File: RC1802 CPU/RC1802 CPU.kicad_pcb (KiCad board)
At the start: 2 copper layers, 99.1 x 99.1 mm, 50 parts, among them J1 Mount, J2 Mount, J3 Mount, J4 Mount, J5 CONN_01X39, J6 CONN_02X20, J7 BARREL_JACK, J8 Conn_CLK, J9 Conn_Q, U1 74LS04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

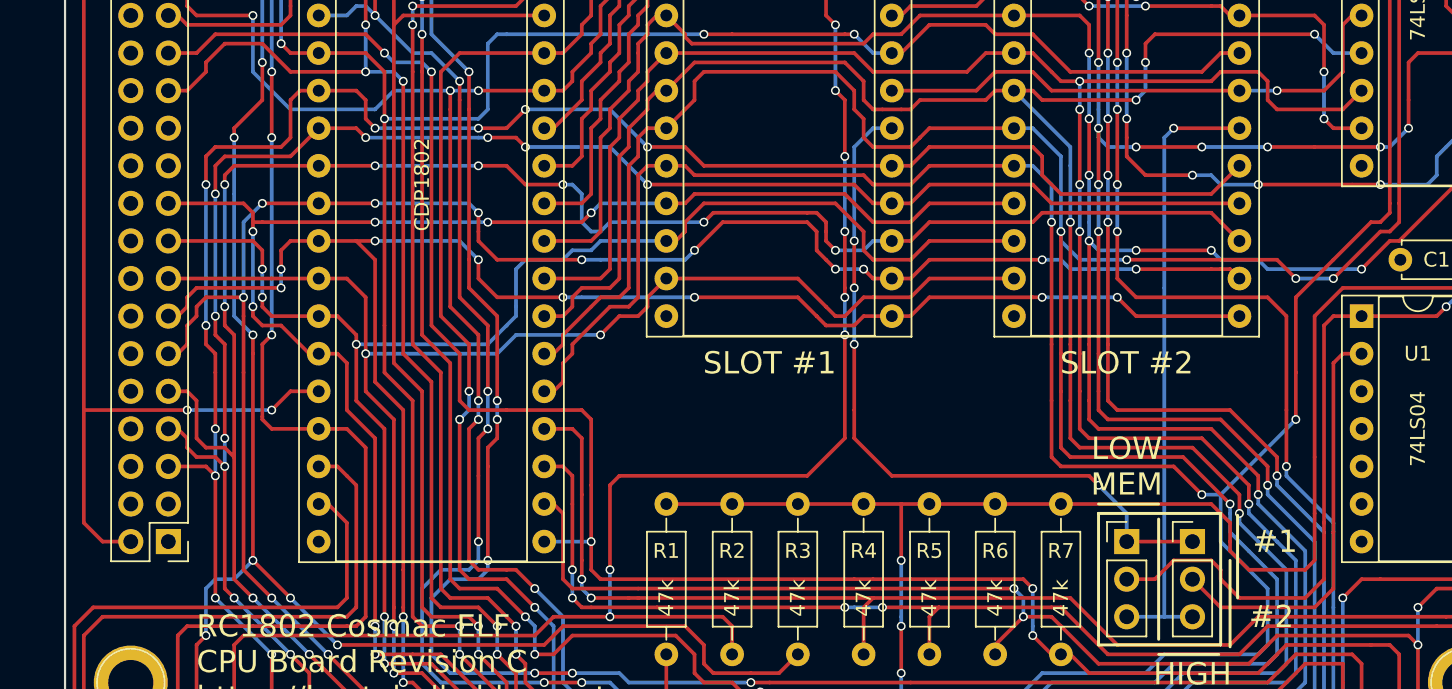
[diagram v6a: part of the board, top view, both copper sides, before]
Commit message: Added ~Q to UI connector
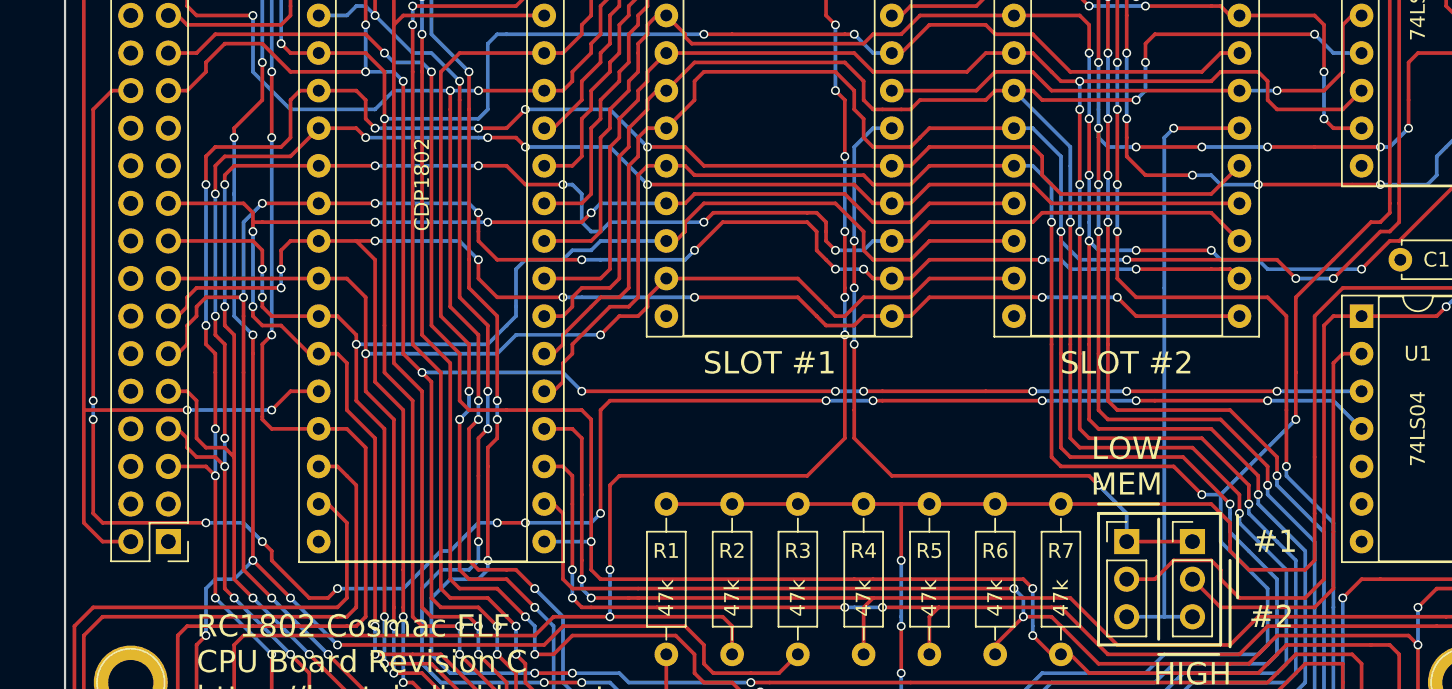
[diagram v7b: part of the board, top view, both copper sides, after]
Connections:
- J6 pad 26: GND -> /~Q
- U1 pad 3: GND -> Q
- U1 pad 4: (no net) -> /~Q
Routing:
- net /~Q: track 0.00 -> 129.2 mm, vias 0 -> 13
- net Q: track 241.1 -> 305.1 mm, vias 9 -> 16
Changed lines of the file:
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@@
     (links 232)
     (no_connects 0)
-    (area 94.275 39.757856 201.735 156.825001)
+    (area 100.209871 48.184999 199.465001 147.395001)
     (thickness 1.6)
     (drawings 150)
-    (tracks 2172)
+    (tracks 2238)
     (zones 0)
     (modules 50)
-    (nets 70)
+    (nets 71)
   )
   (page A4)
@@
   (net 68 "Net-(J8-Pad2)")
   (net 69 "Net-(J8-Pad4)")
+  (net 70 /~Q)
   (net_class Default "This is the default net class."
     (clearance 0.2)
@@
     (add_net /MA8)
     (add_net /MA9)
+    (add_net /~Q)
     (add_net CLOCK)
     (add_net DMA_IN)
@@
       (net 1 GND))
     (pad 3 thru_hole oval (at 0 5.08) (size 1.6 1.6) (drill 0.8) (layers *.Cu *.Mask)
-      (net 1 GND))
+      (net 23 Q))
     (pad 10 thru_hole oval (at 7.62 10.16) (size 1.6 1.6) (drill 0.8) (layers *.Cu *.Mask))
-    (pad 4 thru_hole oval (at 0 7.62) (size 1.6 1.6) (drill 0.8) (layers *.Cu *.Mask))
+    (pad 4 thru_hole oval (at 0 7.62) (size 1.6 1.6) (drill 0.8) (layers *.Cu *.Mask)
+      (net 70 /~Q))
     (pad 11 thru_hole oval (at 7.62 7.62) (size 1.6 1.6) (drill 0.8) (layers *.Cu *.Mask)
       (net 1 GND))
@@
       (net 23 Q))
     (pad 26 thru_hole oval (at 2.54 30.48 180) (size 1.7 1.7) (drill 1) (layers *.Cu *.Mask)
-      (net 1 GND))
+      (net 70 /~Q))
     (pad 27 thru_hole oval (at 0 33.02 180) (size 1.7 1.7) (drill 1) (layers *.Cu *.Mask)
       (net 3 EF4))
@@
   (segment (start 144.145 142.24) (end 140.97 142.24) (width 0.25) (layer F.Cu) (net 22))
   (segment (start 144.78 142.875) (end 144.78 146.05) (width 0.25) (layer F.Cu) (net 22))
+  (segment (start 155.575 121.92) (end 154.305 121.92) (width 0.25) (layer F.Cu) (net 23))
+  (segment (start 187.96 121.92) (end 184.785 121.92) (width 0.25) (layer B.Cu) (net 23))
+  (segment (start 165.735 121.92) (end 162.56 121.92) (width 0.25) (layer F.Cu) (net 23))
+  (via (at 165.735 121.92) (size 0.6) (drill 0.4) (layers F.Cu B.Cu) (net 23))
+  (segment (start 172.085 121.92) (end 165.735 121.92) (width 0.25) (layer B.Cu) (net 23))
+  (via (at 172.085 121.92) (size 0.6) (drill 0.4) (layers F.Cu B.Cu) (net 23))
+  (segment (start 182.245 121.92) (end 172.085 121.92) (width 0.25) (layer F.Cu) (net 23))
+  (via (at 182.245 121.92) (size 0.6) (drill 0.4) (layers F.Cu B.Cu) (net 23))
+  (segment (start 184.785 121.92) (end 182.245 121.92) (width 0.25) (layer B.Cu) (net 23))
+  (segment (start 155.575 121.92) (end 162.56 121.92) (width 0.25) (layer F.Cu) (net 23))
+  (via (at 124.46 120.65) (size 0.6) (drill 0.4) (layers F.Cu B.Cu) (net 23))
+  (segment (start 133.985 120.65) (end 124.46 120.65) (width 0.25) (layer B.Cu) (net 23))
+  (segment (start 135.255 121.92) (end 133.985 120.65) (width 0.25) (layer B.Cu) (net 23))
+  (via (at 135.255 121.92) (size 0.6) (drill 0.4) (layers F.Cu B.Cu) (net 23))
+  (segment (start 152.4 121.92) (end 135.255 121.92) (width 0.25) (layer F.Cu) (net 23))
+  (via (at 152.4 121.92) (size 0.6) (drill 0.4) (layers F.Cu B.Cu) (net 23))
+  (segment (start 154.305 121.92) (end 152.4 121.92) (width 0.25) (layer B.Cu) (net 23))
+  (via (at 154.305 121.92) (size 0.6) (drill 0.4) (layers F.Cu B.Cu) (net 23))
   (segment (start 184.15 48.895) (end 186.055 48.895) (width 0.25) (layer F.Cu) (net 23))
   (via (at 100.965 80.01) (size 0.6) (drill 0.4) (layers F.Cu B.Cu) (net 23))
@@
   (via (at 123.19 100.965) (size 0.6) (drill 0.4) (layers F.Cu B.Cu) (net 23))
   (segment (start 123.19 119.38) (end 123.19 100.965) (width 0.25) (layer F.Cu) (net 23))
-  (segment (start 125.095 121.285) (end 123.19 119.38) (width 0.25) (layer F.Cu) (net 23))
+  (segment (start 125.095 121.285) (end 124.46 120.65) (width 0.25) (layer F.Cu) (net 23))
+  (segment (start 124.46 120.65) (end 123.19 119.38) (width 0.25) (layer F.Cu) (net 23))
   (segment (start 125.095 135.89) (end 125.095 121.285) (width 0.25) (layer F.Cu) (net 23))
   (segment (start 125.73 136.525) (end 125.095 135.89) (width 0.25) (layer F.Cu) (net 23))
@@
   (via (at 128.27 68.58) (size 0.6) (drill 0.4) (layers F.Cu B.Cu) (net 69))
   (segment (start 129.54 67.31) (end 128.27 68.58) (width 0.25) (layer B.Cu) (net 69))
+  (segment (start 118.745 135.255) (end 123.19 135.255) (width 0.25) (layer B.Cu) (net 70))
+  (segment (start 112.395 130.81) (end 113.665 132.08) (width 0.25) (layer B.Cu) (net 70))
+  (via (at 113.665 132.08) (size 0.6) (drill 0.4) (layers F.Cu B.Cu) (net 70))
+  (segment (start 113.665 132.08) (end 114.3 132.715) (width 0.25) (layer F.Cu) (net 70))
+  (segment (start 114.3 132.715) (end 114.3 133.35) (width 0.25) (layer F.Cu) (net 70))
+  (segment (start 114.3 133.35) (end 116.84 135.89) (width 0.25) (layer F.Cu) (net 70))
+  (segment (start 116.84 135.89) (end 118.11 135.89) (width 0.25) (layer F.Cu) (net 70))
+  (segment (start 118.11 135.89) (end 118.745 135.255) (width 0.25) (layer F.Cu) (net 70))
+  (via (at 118.745 135.255) (size 0.6) (drill 0.4) (layers F.Cu B.Cu) (net 70))
+  (segment (start 124.46 133.985) (end 125.73 132.715) (width 0.25) (layer B.Cu) (net 70))
+  (segment (start 125.73 132.715) (end 126.365 132.715) (width 0.25) (layer B.Cu) (net 70))
+  (segment (start 126.365 132.715) (end 128.27 130.81) (width 0.25) (layer B.Cu) (net 70))
+  (segment (start 128.27 130.81) (end 129.54 130.81) (width 0.25) (layer B.Cu) (net 70))
+  (segment (start 135.89 130.81) (end 131.445 130.81) (width 0.25) (layer B.Cu) (net 70))
+  (segment (start 103.505 101.6) (end 102.235 102.87) (width 0.25) (layer F.Cu) (net 70))
+  (segment (start 102.235 102.87) (end 102.235 122.555) (width 0.25) (layer F.Cu) (net 70))
+  (via (at 102.235 122.555) (size 0.6) (drill 0.4) (layers F.Cu B.Cu) (net 70))
+  (segment (start 102.235 122.555) (end 102.235 123.825) (width 0.25) (layer B.Cu) (net 70))
+  (via (at 102.235 123.825) (size 0.6) (drill 0.4) (layers F.Cu B.Cu) (net 70))
+  (segment (start 102.235 123.825) (end 102.235 130.175) (width 0.25) (layer F.Cu) (net 70))
+  (segment (start 102.235 130.175) (end 102.87 130.81) (width 0.25) (layer F.Cu) (net 70))
+  (segment (start 102.87 130.81) (end 109.855 130.81) (width 0.25) (layer F.Cu) (net 70))
+  (via (at 109.855 130.81) (size 0.6) (drill 0.4) (layers F.Cu B.Cu) (net 70))
+  (segment (start 135.89 130.81) (end 136.525 130.175) (width 0.25) (layer B.Cu) (net 70))
+  (via (at 136.525 130.175) (size 0.6) (drill 0.4) (layers F.Cu B.Cu) (net 70))
+  (segment (start 136.525 130.175) (end 136.525 123.19) (width 0.25) (layer F.Cu) (net 70))
+  (segment (start 136.525 123.19) (end 137.16 122.555) (width 0.25) (layer F.Cu) (net 70))
+  (segment (start 137.16 122.555) (end 151.765 122.555) (width 0.25) (layer F.Cu) (net 70))
+  (via (at 151.765 122.555) (size 0.6) (drill 0.4) (layers F.Cu B.Cu) (net 70))
+  (segment (start 151.765 122.555) (end 154.94 122.555) (width 0.25) (layer B.Cu) (net 70))
+  (via (at 154.94 122.555) (size 0.6) (drill 0.4) (layers F.Cu B.Cu) (net 70))
+  (segment (start 154.94 122.555) (end 155.575 122.555) (width 0.25) (layer F.Cu) (net 70))
+  (segment (start 173.99 122.555) (end 172.72 122.555) (width 0.25) (layer F.Cu) (net 70))
+  (segment (start 186.055 122.555) (end 181.61 122.555) (width 0.25) (layer B.Cu) (net 70))
+  (via (at 181.61 122.555) (size 0.6) (drill 0.4) (layers F.Cu B.Cu) (net 70))
+  (segment (start 181.61 122.555) (end 173.99 122.555) (width 0.25) (layer F.Cu) (net 70))
+  (segment (start 187.96 124.46) (end 186.055 122.555) (width 0.25) (layer B.Cu) (net 70))
+  (segment (start 166.37 122.555) (end 155.575 122.555) (width 0.25) (layer F.Cu) (net 70))
+  (via (at 166.37 122.555) (size 0.6) (drill 0.4) (layers F.Cu B.Cu) (net 70))
+  (segment (start 172.72 122.555) (end 166.37 122.555) (width 0.25) (layer B.Cu) (net 70))
+  (via (at 172.72 122.555) (size 0.6) (drill 0.4) (layers F.Cu B.Cu) (net 70))
+  (segment (start 103.505 101.6) (end 104.775 101.6) (width 0.25) (layer F.Cu) (net 70) (status 800000))
+  (via (at 129.54 130.81) (size 0.6) (drill 0.4) (layers F.Cu B.Cu) (net 70))
+  (segment (start 131.445 130.81) (end 129.54 130.81) (width 0.25) (layer F.Cu) (net 70))
+  (via (at 131.445 130.81) (size 0.6) (drill 0.4) (layers F.Cu B.Cu) (net 70))
+  (segment (start 109.855 130.81) (end 112.395 130.81) (width 0.25) (layer B.Cu) (net 70))
+  (segment (start 123.19 135.255) (end 124.46 133.985) (width 0.25) (layer B.Cu) (net 70))
   (zone (net 1) (net_name GND) (layer B.Cu) (hatch edge 0.508)
     (connect_pads (clearance 0.508))

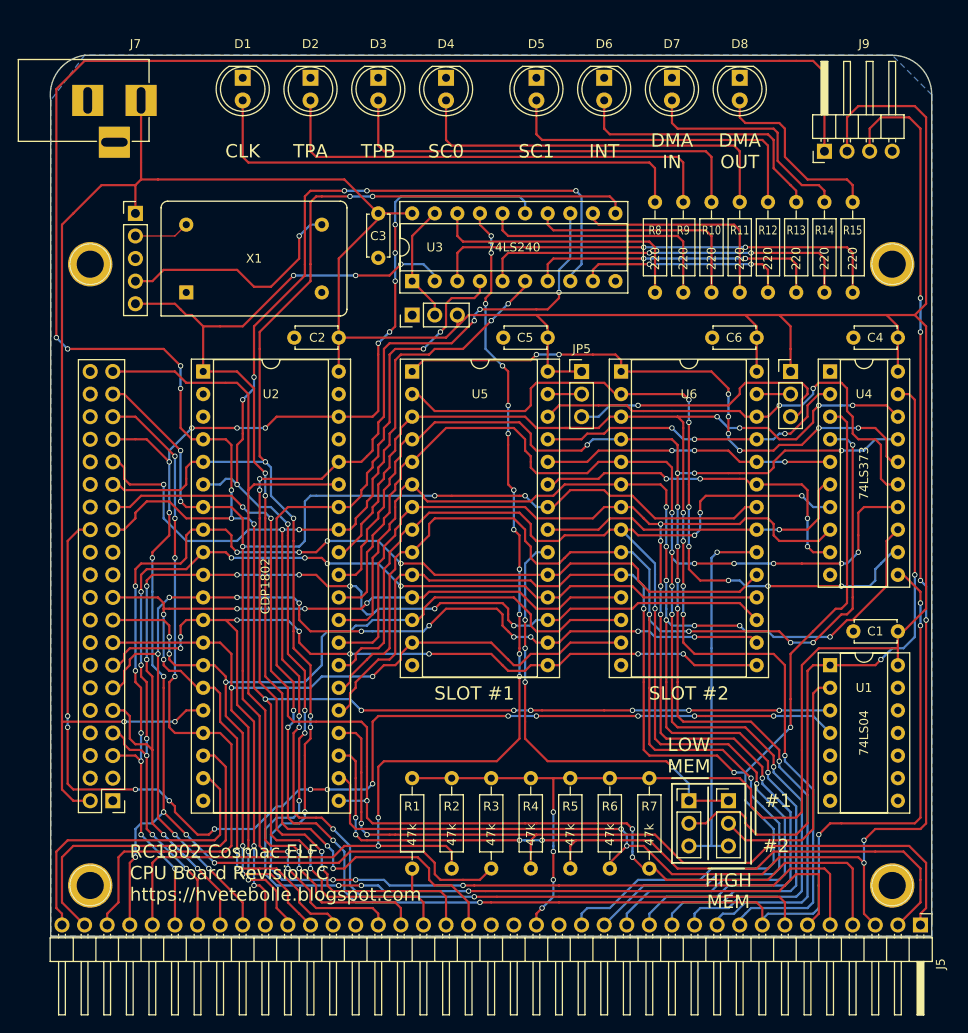
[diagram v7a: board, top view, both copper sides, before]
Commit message: Fixed tracks missing due to labelling issues
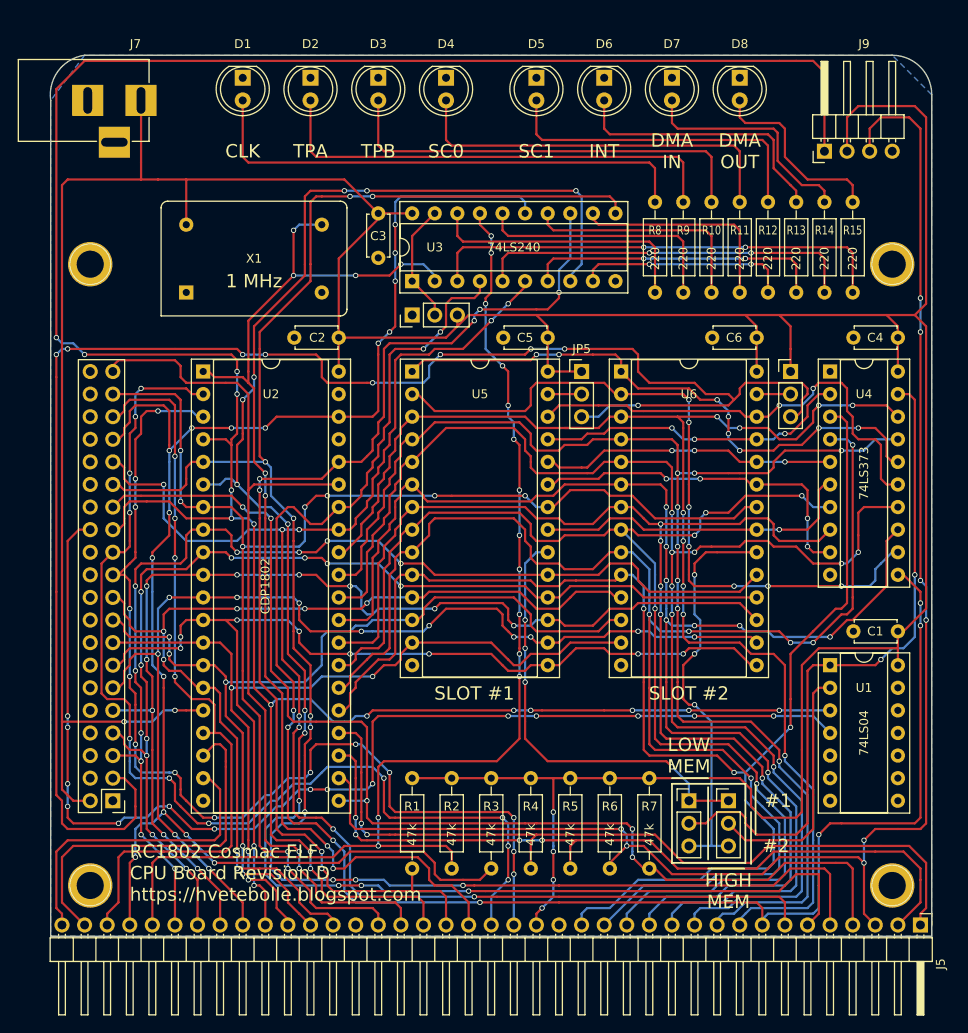
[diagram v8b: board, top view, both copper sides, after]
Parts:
- removed J8: Conn_CLK, Pin_Headers:Pin_Header_Straight_1x05_Pitch2.54mm
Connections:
- J5 pad 19: (no net) -> ~CLEAR
- J5 pad 20: (no net) -> ~WAIT
- J6 pad 10: GND -> (no net)
- J6 pad 12: GND -> (no net)
- J6 pad 14: GND -> (no net)
- J6 pad 16: GND -> (no net)
- J6 pad 18: GND -> (no net)
- J6 pad 20: GND -> (no net)
- J6 pad 21: (no net) -> ~CLEAR
- J6 pad 22: GND -> (no net)
- J6 pad 23: (no net) -> ~WAIT
- J6 pad 24: GND -> (no net)
- J6 pad 28: GND -> (no net)
- J6 pad 3: (no net) -> MP
- J6 pad 30: GND -> (no net)
- J6 pad 32: GND -> (no net)
- J6 pad 34: GND -> (no net)
- JP4 pad 3: ~WE -> MP
- JP5 pad 3: ~WE -> MP
- U2 pad 2: (no net) -> ~WAIT
- U2 pad 3: (no net) -> ~CLEAR
- X1 pad 14: Net-(J8-Pad2) -> VCC
- X1 pad 8: Net-(J8-Pad4) -> CLOCK
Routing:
- net MP: track 0.00 -> 185.2 mm, vias 0 -> 9
- net ~WAIT: track 0.00 -> 121.4 mm, vias 0 -> 11
- net ~CLEAR: track 0.00 -> 119.0 mm, vias 0 -> 14
- net ~WE: track 31.9 -> 0.00 mm, vias 1 -> 0
- net Net-(J8-Pad4): track 26.7 -> 0.00 mm, vias 1 -> 0
- net Q: track 305.1 -> 312.4 mm
- net DMA_IN: track 172.7 -> 179.1 mm
- net Net-(J8-Pad2): track 6.24 -> 0.00 mm
- net N2: track 80.1 -> 84.7 mm
- net VCC: track 428.5 -> 433.0 mm
- net SLOT2_CS: track 42.2 -> 46.4 mm, vias 1 -> 3
- net CLOCK: track 130.6 -> 127.1 mm, vias 7 -> 8
- net MRD: track 146.9 -> 149.9 mm, vias 7 -> 9
- net /~Q: track 129.2 -> 132.2 mm, vias 13 -> 15
- net /BUS5: track 125.9 -> 123.1 mm, vias 9 -> 10
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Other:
- board text added: "1 MHz"
- board text added: "CLOCK"
- board text added: "RC1802 Cosmac ELF CPU Board Revision D https://hvetebolle.blogspot.com"
- board text removed: "ENABLE"
- board text removed: "POWER"
- board text removed: "RC1802 Cosmac ELF CPU Board Revision C https://hvetebolle.blogspot.com"
